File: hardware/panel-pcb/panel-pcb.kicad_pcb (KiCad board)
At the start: 4 copper layers, 135.5 x 127 mm, 134 parts, among them J1 USB_C_Receptacle_USB2.0_16P, J10 RS-485 OUT, J11 12V_OUT, J2 SWD, J3 FSR North, J4 FSR East, J5 12V_IN, J6 FSR South, J7 FSR West, J8 RS-485 IN, J9 INT OUT, SW1 PANEL_ID, SW2 BOOTSEL, SW3 RS-485 Termination, U1 RP2040, U2 THVD1419, U3 W25Q32JV, U4 SN74AHCT125, U5 AMS1117-5.0, U6 AP7361C-33ER-13, U7 USBLC6-2SC6, X1 12MHz ABM8-272-T3

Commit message: Panel PCB: board art, name/rev silk, follow-up review fixes
- Silkscreen: 'Kraken Pad by SenPi / Rev. 1.0' (F.Silk), JLC order-number
  placeholder JLCJLCJLCJLC (B.Silk).
- Personal logo as exposed copper: 5 poly pairs F.Cu + point-registered
  F.Mask openings; degenerate near-zero-area sliver pair deleted
  (follow-up review F3).
- R19 22k -> 33k: 12V-sense node ~2.98V, ~1V margin over guaranteed
  2.0V VIH (follow-up review F1; old 22k value had 164mV nominal margin).
- New D29 PMEG3015EH clamp, anode GPIO17 / cathode +3V3: bounds the
  sense node to one Vf above the rail when IOVDD is down, closing the
  RP2040 abs-max-vs-FT-description ambiguity (follow-up review F2).
- Via DRC rules switched to JLC 4-layer standard class (0.3mm drill /
  0.45mm dia) - board passes clean, no premium via process needed.

ERC: 1 warning (D29 cached D_Schottky lib_symbol_mismatch, known noise
class). DRC 0 violations, 0 unconnected.
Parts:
- added D29: PMEG3015EH, Diode_SMD:D_SOD-123F, F.Cu at (189.7, 92.9)
- R19: value 22k -> 33k
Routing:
- net +3V3: track 48.7 -> 50.2 mm, vias 32 -> 33
- net GND: vias 394 -> 186
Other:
- board text added: "JLCJLCJLCJLC"
- board text added: "Kraken Pad by SenPi Rev. 1.0"

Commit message: Panel PCB: LCSC part numbers, 200R fix, pre-order checklist
- LCSC fields added to all SMD symbols from the JLC quote session's
  matched picks (tmp/bom.xls) - BOM/CPL exports now carry exact part
  numbers so re-uploads auto-match without manual picking.
- R5 201R -> 200R 1%: JLC stocks no 201R; the matched part (C8218) is
  200R, and the ADC_AVDD filter doesn't care. Value now matches reality.
- R7/R15 1k -> '1k 1%' so all three 1k positions (with R6) merge to one
  BOM line, matching the single part picked for them (C2907002).
- D29 Description filled (12V-sense clamp role); stray trailing quote
  removed. TP6 'RS-485 DC' -> 'DE' typo fixed.
- docs/PRE_ORDER_CHECKLIST.md: full pre-order runbook - physical part
  verifies (J9/PHR-2/SW footprints), BOM-confirm and rotation-preview
  gotchas, order options with measured qty-5 cost structure (~$148
  fixed overhead -> order all boards in one run), bring-up list.

ERC 0 errors; DRC 0 errors (known benign warnings only).
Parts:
- R15, R7: value 1k -> 1k 1%
- R5: value 201R 1% -> 200R 1%

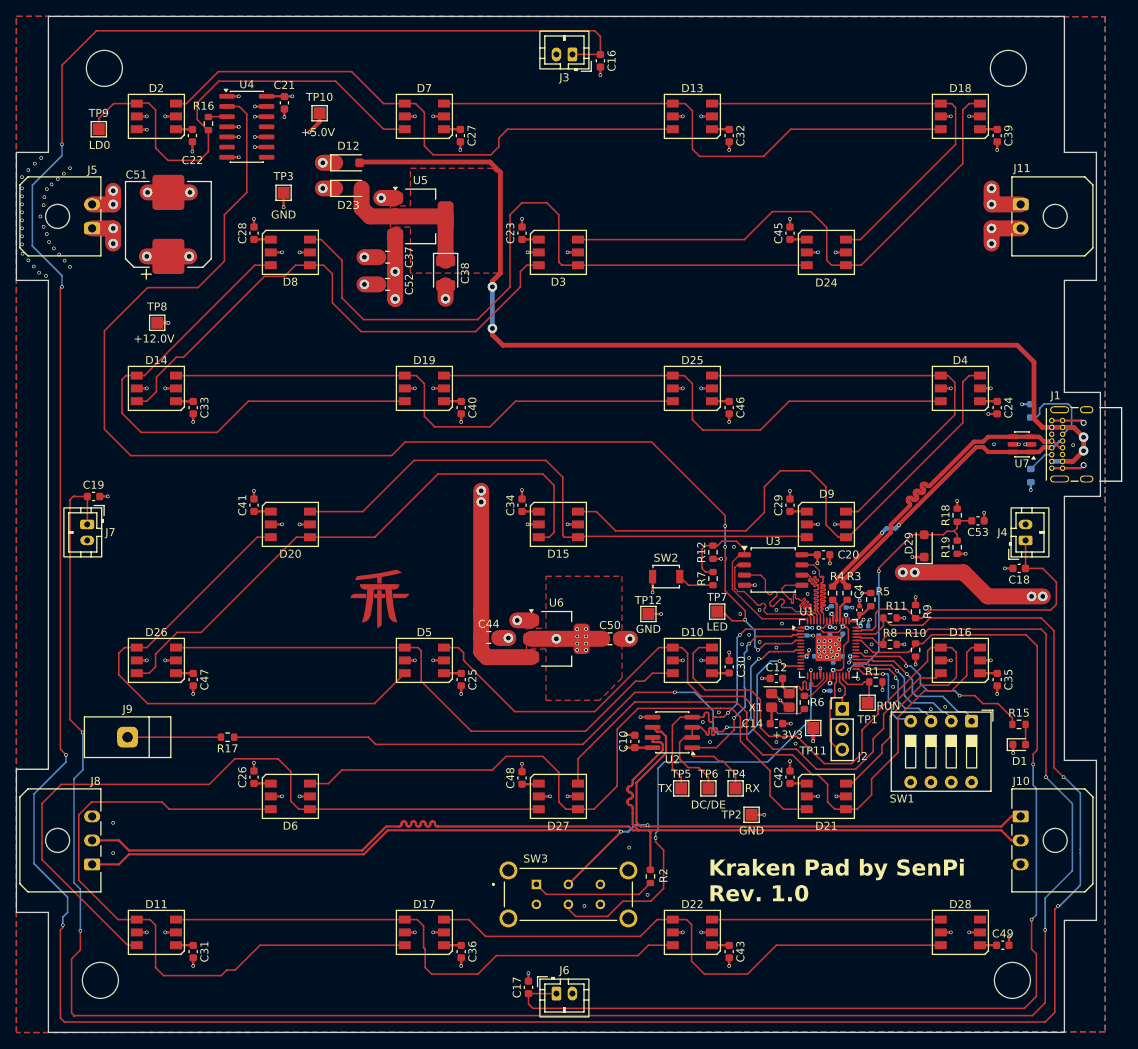
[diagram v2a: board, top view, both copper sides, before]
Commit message: README: AI disclosure section; Panel PCB: via update
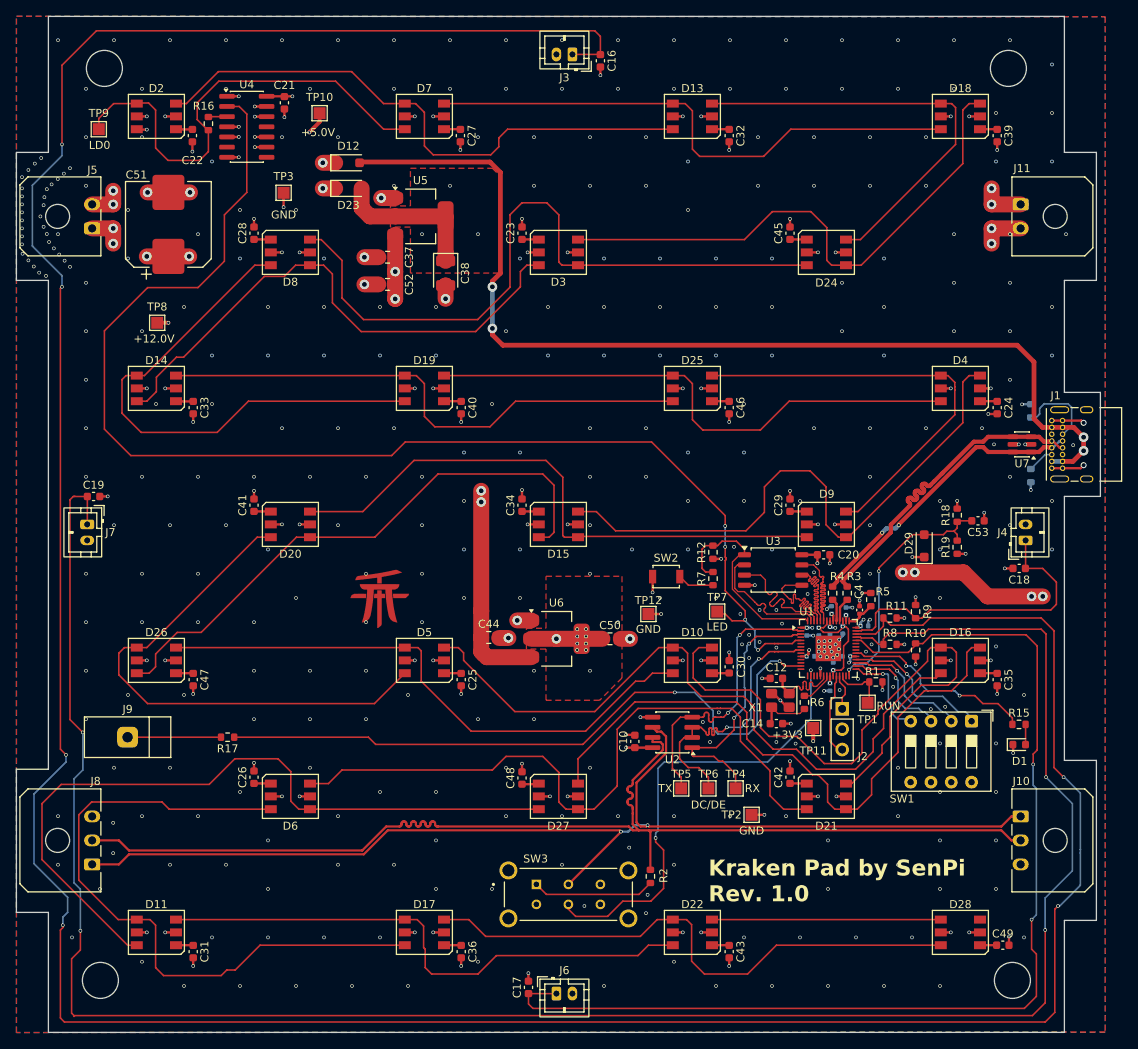
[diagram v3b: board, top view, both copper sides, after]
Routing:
- net GND: vias 186 -> 463
